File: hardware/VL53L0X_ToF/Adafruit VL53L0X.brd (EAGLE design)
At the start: 100 x 80 mm, 17 parts, among them Q1 BSS138, Q2 BSS138, U1 VL53L0X, U2 MIC5225_2.8V

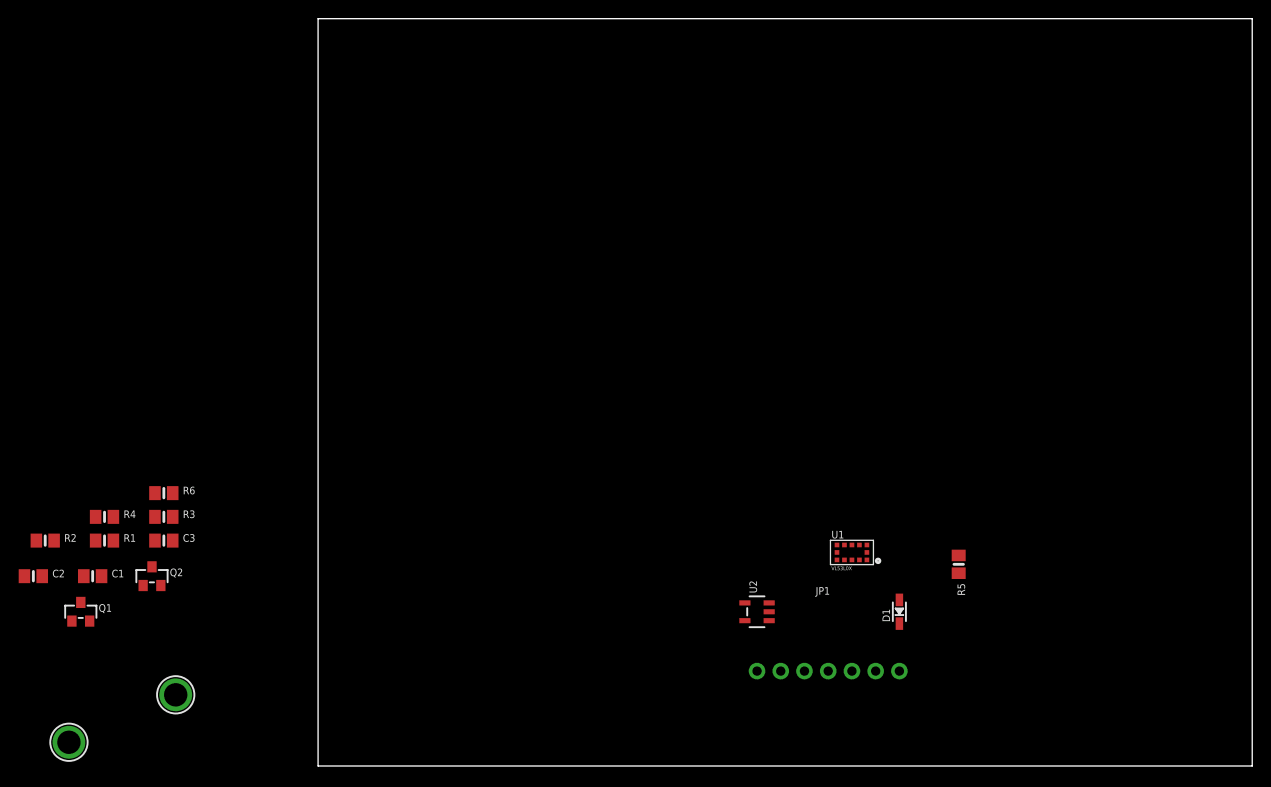
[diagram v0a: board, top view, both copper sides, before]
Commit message: revert to original design by adafruit
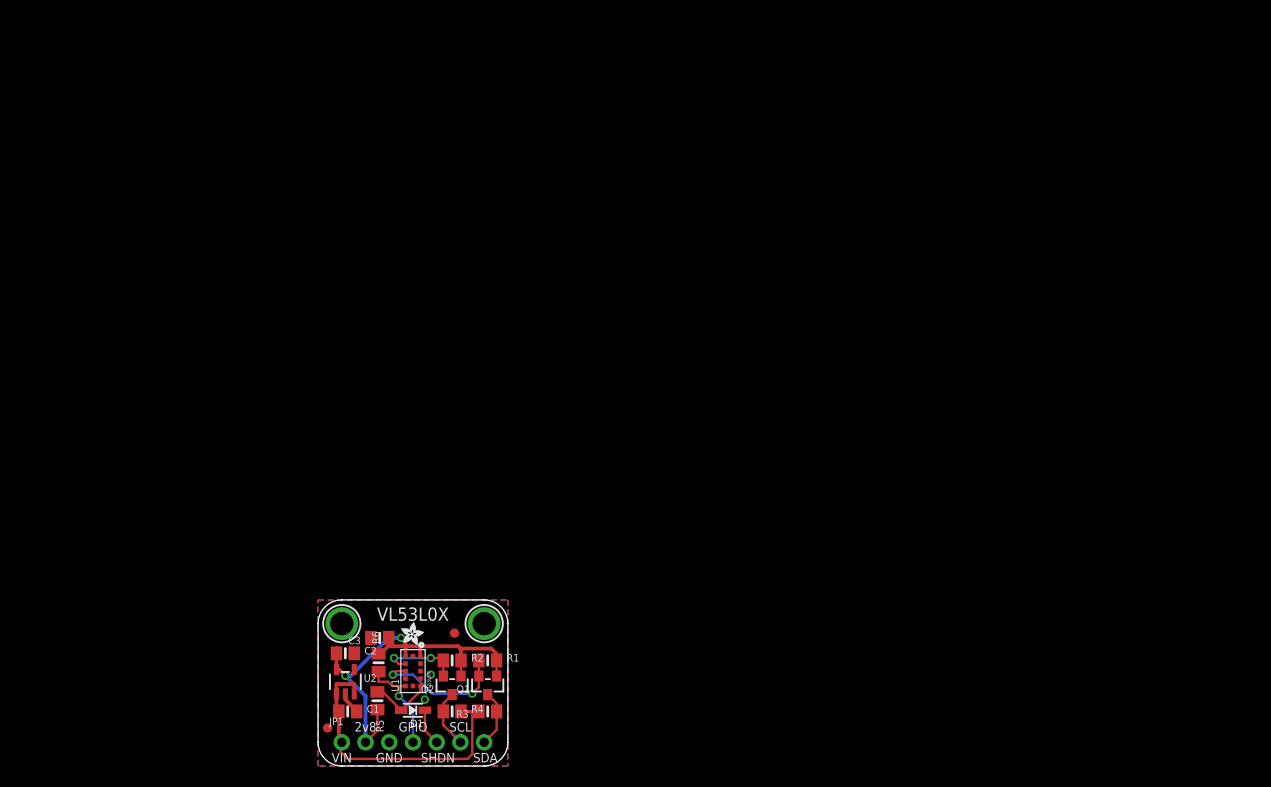
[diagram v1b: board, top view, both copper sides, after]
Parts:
- added FID2, FID3: FIDUCIAL"", microbuilder:FIDUCIAL_1MM
- added U$12: (no value), microbuilder:PCBFEAT-REV-040
- added U$15: (no value), microbuilder:ADAFRUIT_3.5MM
- added U$18: (no value), microbuilder:ADAFRUIT_2.5MM
- moved R5 63.9 mm to (6.35, 6.99)
- moved D1 53.1 mm to (10.2, 5.97), turned to 180 degrees
- moved U1 48.7 mm to (10.2, 10.2), turned to 90 degrees
- moved R2 45.4 mm to (14.4, 11.3)
- moved JP1 45.1 mm to (10.2, 2.54)
- moved U2 44.7 mm to (2.92, 9.02), turned to 0 degrees
- moved Q1 44.3 mm to (18.2, 8.64), turned to 180 degrees
- moved R1 43.0 mm to (18.2, 11.3)
- moved R4 42.6 mm to (14.4, 5.84)
- moved R3 40.4 mm to (18.2, 5.84), turned to 180 degrees
- moved C2 34.4 mm to (2.92, 12.1)
- moved Q2 34.2 mm to (14.4, 8.64), turned to 180 degrees
- moved U$14 33.9 mm to (17.8, 15.2)
- moved U$13 31.9 mm to (2.54, 15.2)
- moved C1 30.9 mm to (3.17, 5.84)
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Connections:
- net SDA: now also JP1.7; no longer JP1.5
- net XSHUT: now also JP1.5; no longer JP1.7
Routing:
- net 2.8V: track 0.00 -> 45.9 mm, vias 0 -> 2
- net VIN: track 0.00 -> 32.8 mm
- net SDA_2.8V: track 0.00 -> 14.7 mm, vias 0 -> 2
- net GPIO: track 0.00 -> 10.8 mm, vias 0 -> 1
- net SCL_2.8V: track 0.00 -> 8.63 mm, vias 0 -> 2
- net XSHUT_2.8V: track 0.00 -> 6.80 mm
- net SCL: track 0.00 -> 6.25 mm
- net SDA: track 0.00 -> 6.04 mm
- net XSHUT: track 0.00 -> 3.96 mm
- net GND: track 0.00 -> 2.84 mm, vias 0 -> 2
- added copper zone on layer 1, net GND
- added copper zone on layer 16, net GND
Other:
- board size 100 x 80 mm -> 20.3 x 17.8 mm
- board text added: "2v8"
- board text added: "GND"
- board text added: "GPIO"
- board text added: "Range ~30-1000mm"
- board text added: "SCL"
- board text added: "SDA"
- board text added: "SHDN"
- board text added: "Time-of-Flight Distance Sensor"
- board text added: "VIN"
- board text added: "VL53L0X"
- board text added: "Vin:3-5V"
- board text added: "Vlogic:3-5V"
